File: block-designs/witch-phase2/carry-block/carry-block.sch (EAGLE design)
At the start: 13 parts, among them IC1 74AHC1G32DBV, IC2 74AHC1G86DBV, IC3 74LS195D, IC4 741G175

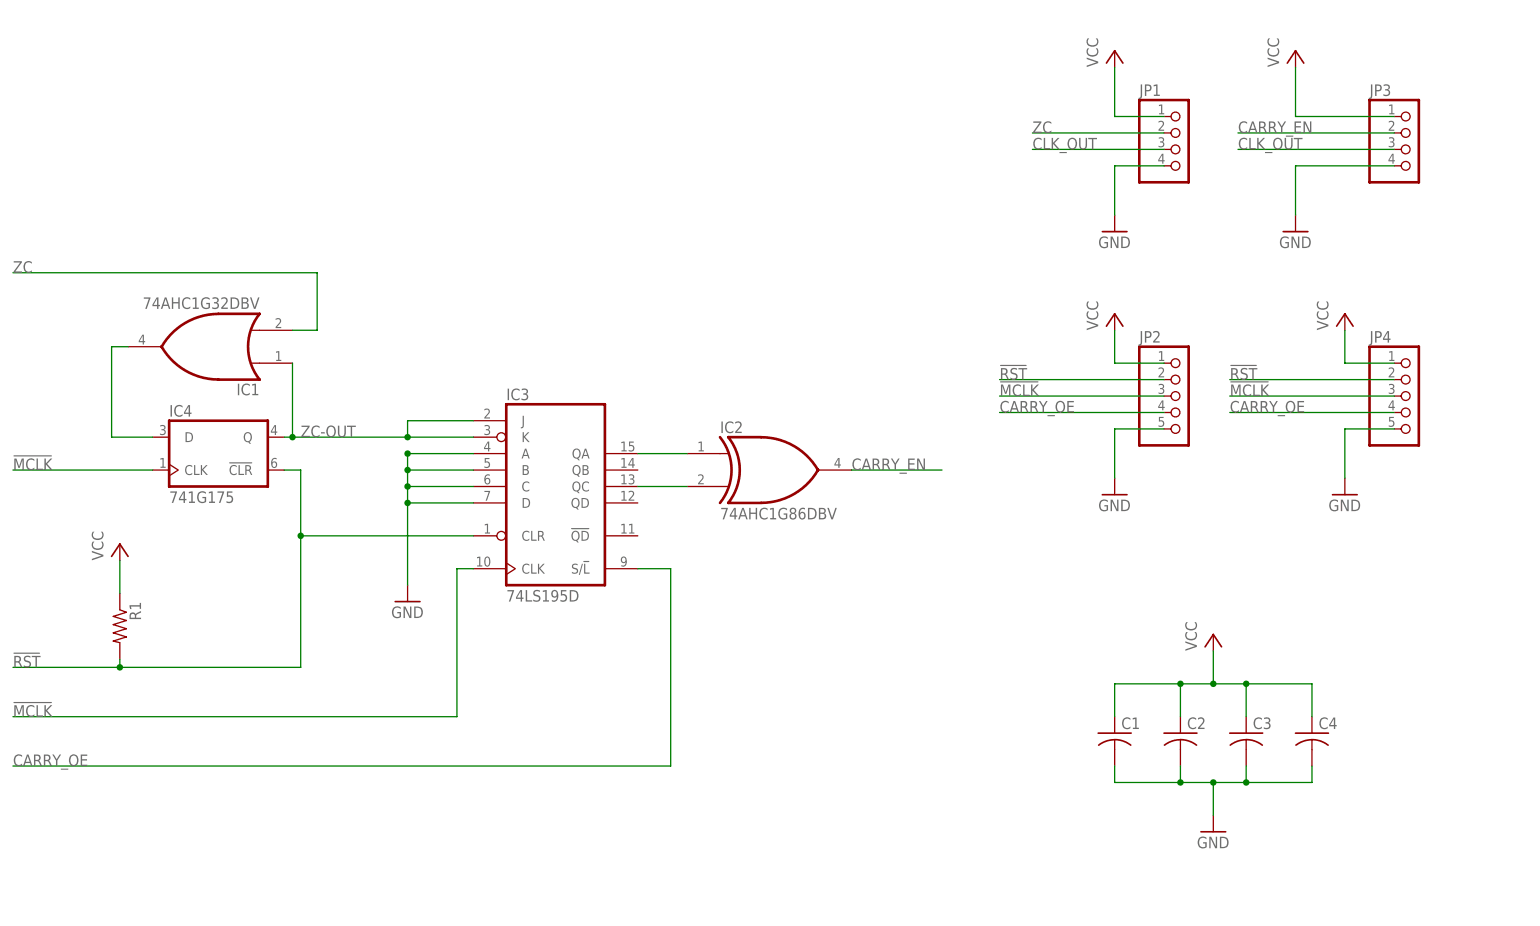
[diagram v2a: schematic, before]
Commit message: updated designs for new labeling and spacing
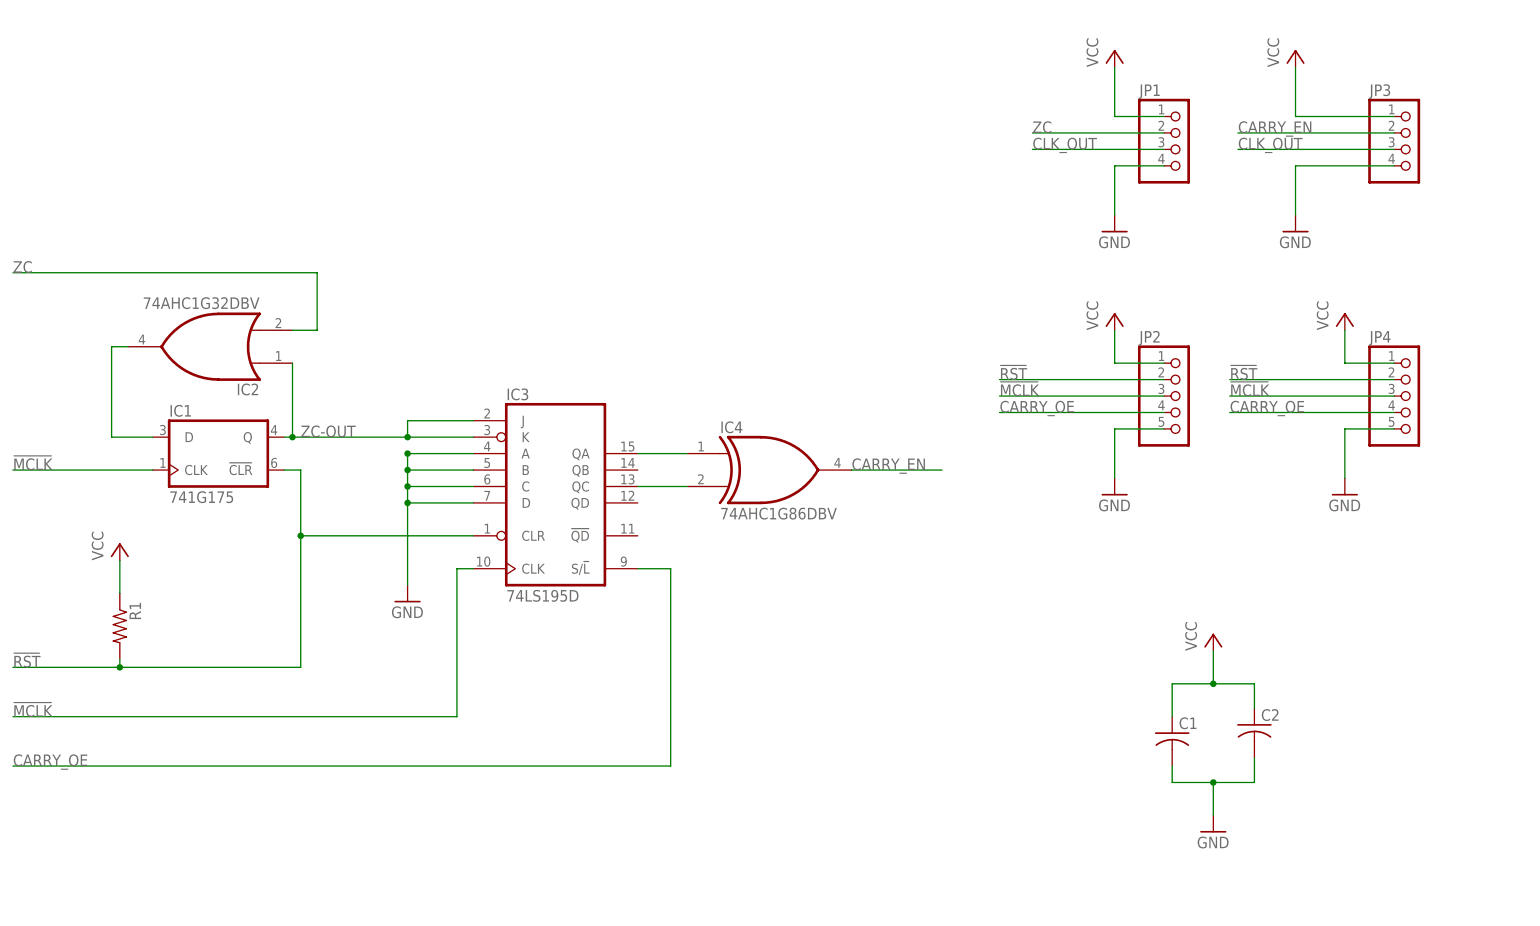
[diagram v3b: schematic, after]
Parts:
- removed C3, C4: (no value), resistor:C-USC0805
- IC1: value 74AHC1G32DBV -> 741G175; device 74xx-little-us:74AHC1G32DBV -> 74xx-little-us:741G175
- IC2: value 74AHC1G86DBV -> 74AHC1G32DBV; device 74xx-little-us:74AHC1G86DBV -> 74xx-little-us:74AHC1G32DBV
- IC4: value 741G175 -> 74AHC1G86DBV; device 74xx-little-us:741G175 -> 74xx-little-us:74AHC1G86DBV
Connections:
- net !MCLK: now also IC1G$1.CLK; no longer IC4G$1.CLK
- net !RST: now also IC1G$1.!CLR; no longer IC4G$1.!CLR
- net CARRY_EN: now also IC4A.O; no longer IC2A.O
- net GND: no longer C3.2, C4.2
- net N$1: now also IC4A.I0; no longer IC2A.I0
- net N$2: now also IC4A.I1; no longer IC2A.I1
- net N$5: now also IC1G$1.D, IC2A.O; no longer IC1A.O, IC4G$1.D
- net VCC: no longer C3.1, C4.1
- net ZC: now also IC2A.I1; no longer IC1A.I1
- net ZC-OUT: now also IC1G$1.Q, IC2A.I0; no longer IC1A.I0, IC4G$1.Q
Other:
- moved on the sheet: C1, C2

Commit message: replace or with d-flipflop to fix zc start issue
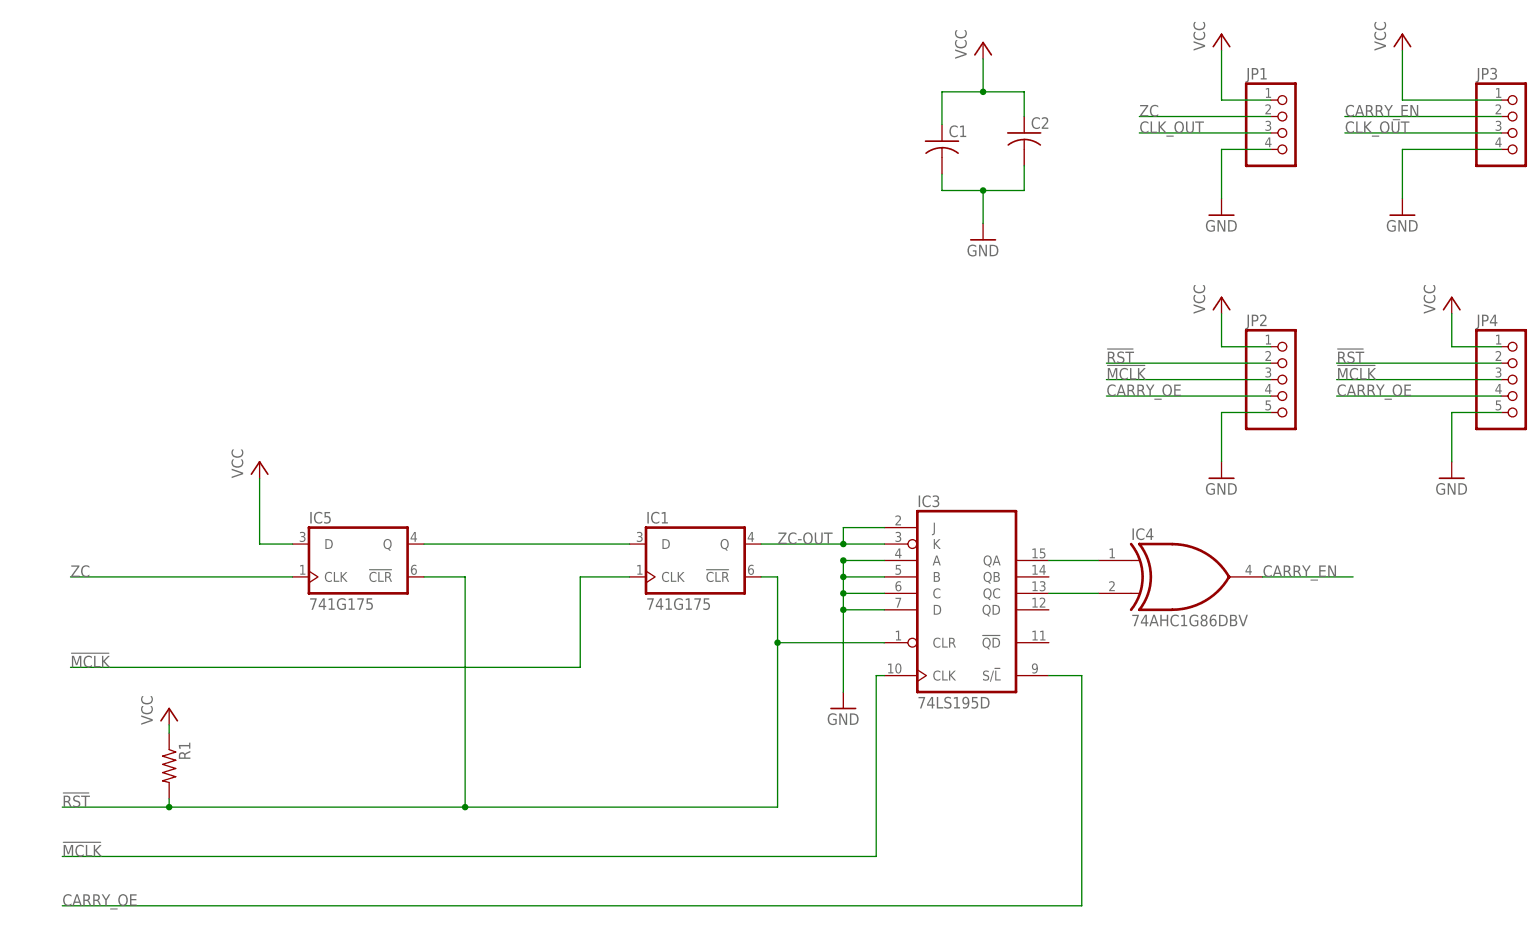
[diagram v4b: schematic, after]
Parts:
- removed IC2: 74AHC1G32DBV, 74xx-little-us:74AHC1G32DBV
- added IC5: 741G175, 74xx-little-us:741G175
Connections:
- net !RST: now also IC5G$1.!CLR
- net N$5: now also IC5G$1.Q; no longer IC2A.O
- net VCC: now also IC5G$1.D
- net ZC: now also IC5G$1.CLK; no longer IC2A.I1
- net ZC-OUT: no longer IC2A.I0
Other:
- moved on the sheet: C1, C2, IC1, IC3, IC4, JP1, JP2, JP3, JP4, R1
